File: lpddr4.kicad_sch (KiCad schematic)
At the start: 43 parts, among them U1 MT53E1G32D2NP-046

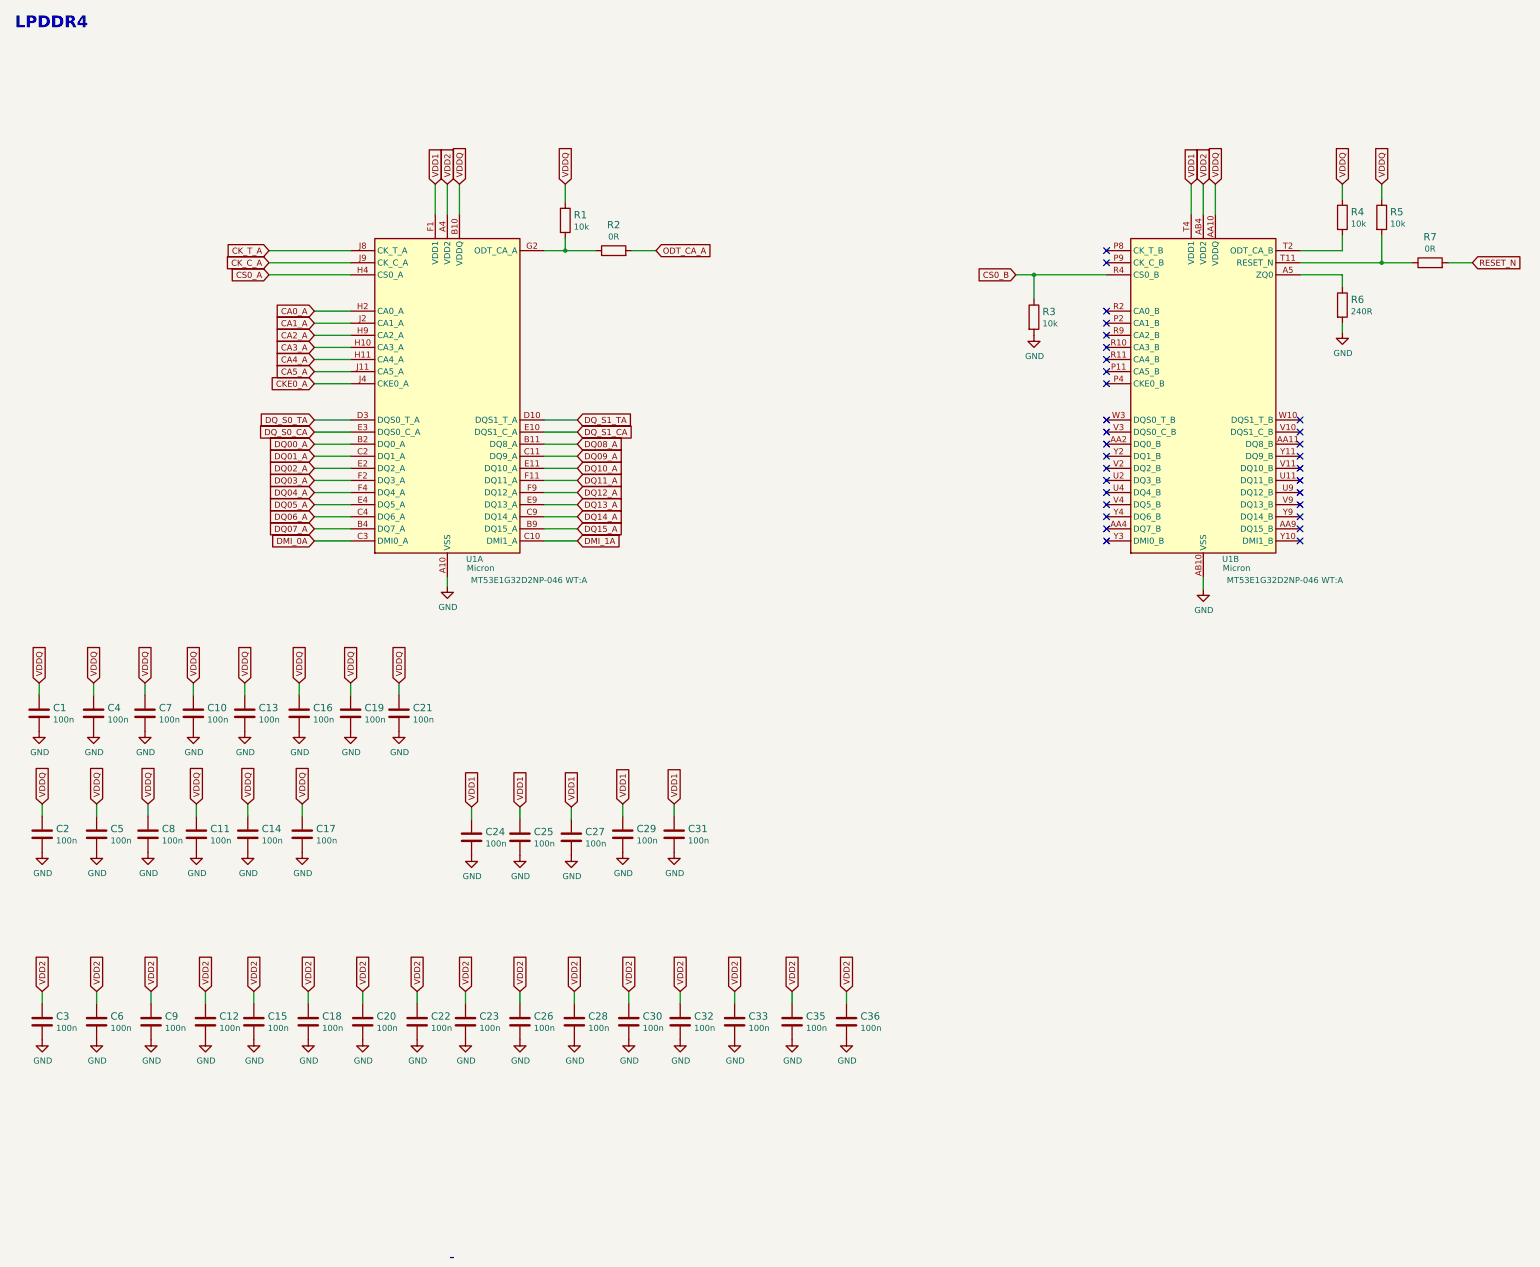
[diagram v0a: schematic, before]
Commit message: Update symbols from library, redo designators
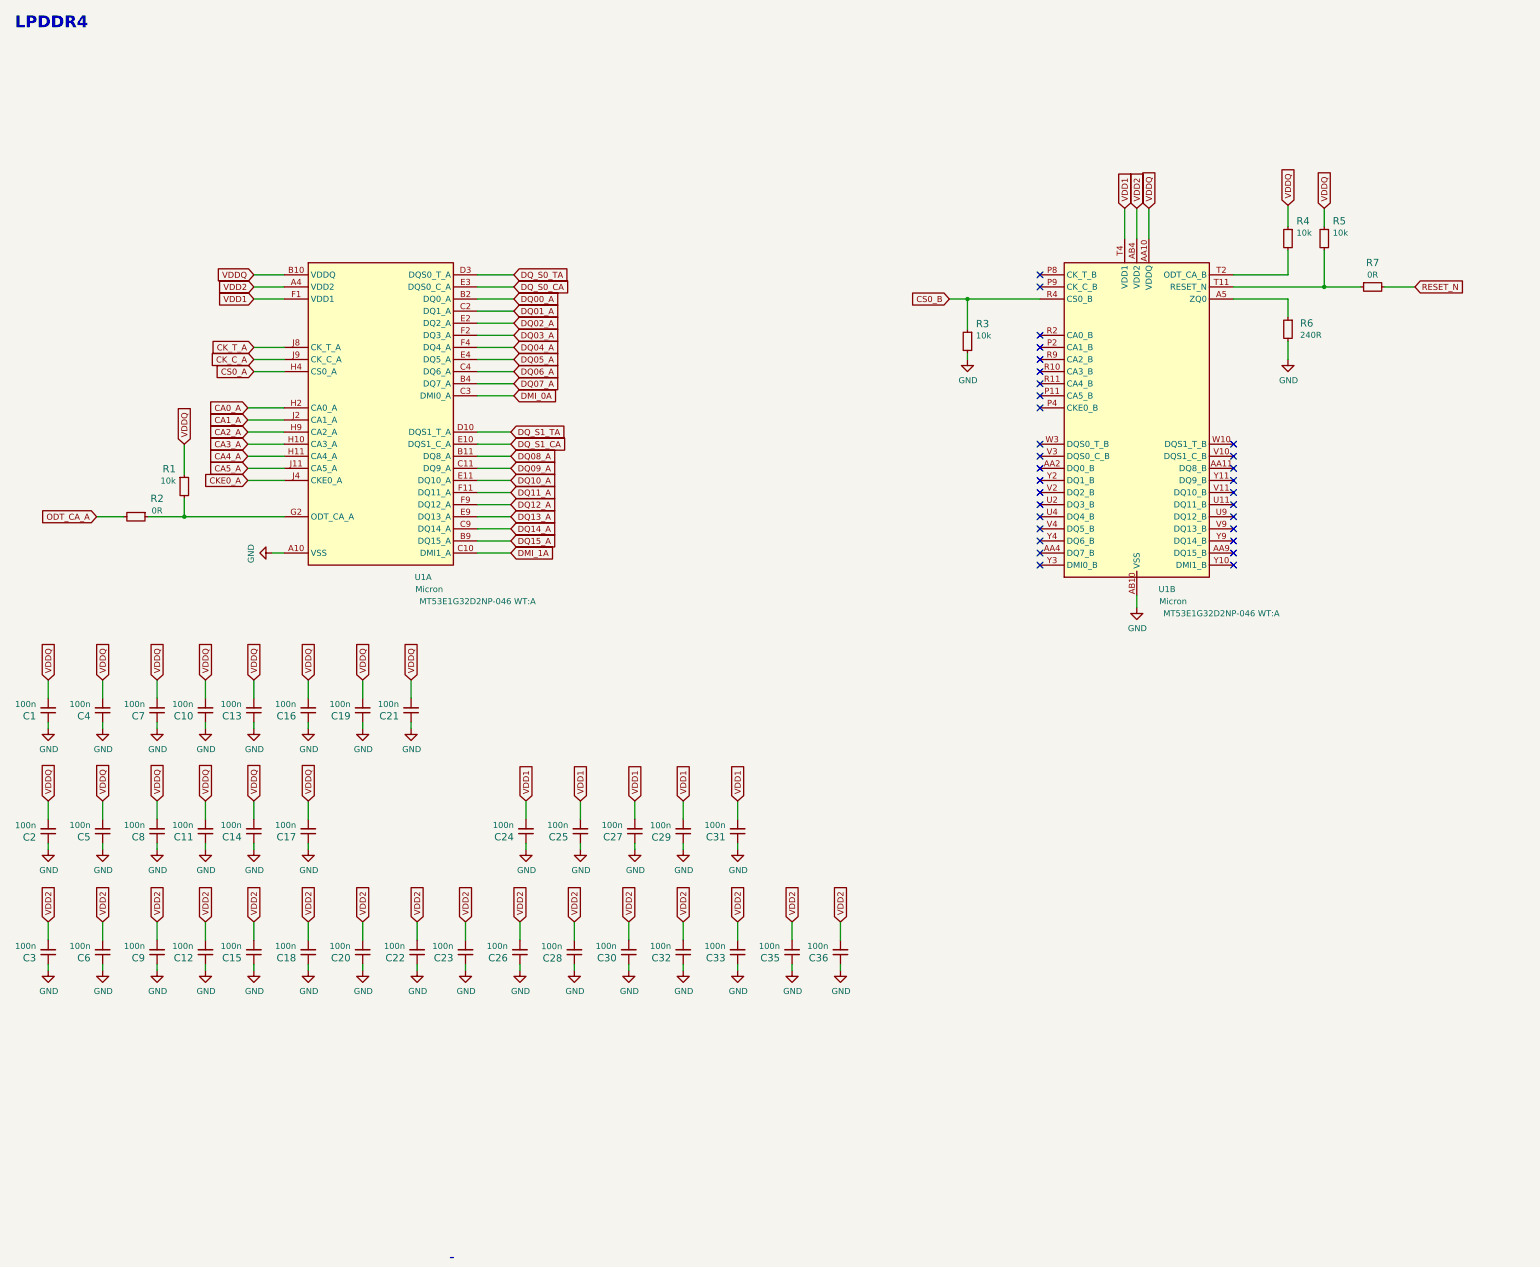
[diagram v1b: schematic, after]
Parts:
- C1, C10, C11, C12, C13, C14, C15, C16, C17, C18, C19, C2, C20, C21, C22, C23, C24, C25, C26, C27, C28, C29, C3, C30, C31, C32, C33, C35, C36, C4, C5, C6, C7, C8, C9: Author (none) -> Antmicro; License (none) -> Apache-2.0; Manufacturer YAGEO -> Yaego
- R1, R3, R4, R5: Author (none) -> Antmicro; License (none) -> Apache-2.0; MPN CRCW040210K0FKEDHP -> CR0402-FX-1002GLF; Manufacturer VISHAY -> Bourns; Tolerance (none) -> 1%
- R2, R7: Author (none) -> Antmicro; Current (none) -> 1A; License (none) -> Apache-2.0; Manufacturer PANASONIC -> Panasonic
- R6: Author (none) -> Antmicro; License (none) -> Apache-2.0; MPN ERJ2GEJ241X -> CR0402-FX-2400GLF; Manufacturer PANASONIC -> Bourns; Tolerance (none) -> 1%
- U1: Author (none) -> Antmicro; License (none) -> Apache-2.0
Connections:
- net GND: now also C1.1, C10.1, C11.1, C12.1, C13.1, C14.1, C15.1, C16.1, C17.1, C18.1, C19.1, C2.1, C20.1, C21.1, C22.1, C23.1, C24.1, C25.1, C26.1, C27.1, C28.1, C29.1, C3.1, C30.1, C31.1, C32.1, C33.1, C35.1, C36.1, C4.1, C5.1, C6.1, C7.1, C8.1, C9.1; no longer C1.2, C10.2, C11.2, C12.2, C13.2, C14.2, C15.2, C16.2, C17.2, C18.2, C19.2, C2.2, C20.2, C21.2, C22.2, C23.2, C24.2, C25.2, C26.2, C27.2, C28.2, C29.2, C3.2, C30.2, C31.2, C32.2, C33.2, C35.2, C36.2, C4.2, C5.2, C6.2, C7.2, C8.2, C9.2
- net VDD1: now also C24.2, C25.2, C27.2, C29.2, C31.2; no longer C24.1, C25.1, C27.1, C29.1, C31.1
- net VDD2: now also C12.2, C15.2, C18.2, C20.2, C22.2, C23.2, C26.2, C28.2, C3.2, C30.2, C32.2, C33.2, C35.2, C36.2, C6.2, C9.2; no longer C12.1, C15.1, C18.1, C20.1, C22.1, C23.1, C26.1, C28.1, C3.1, C30.1, C32.1, C33.1, C35.1, C36.1, C6.1, C9.1
- net VDDQ: now also C1.2, C10.2, C11.2, C13.2, C14.2, C16.2, C17.2, C19.2, C2.2, C21.2, C4.2, C5.2, C7.2, C8.2; no longer C1.1, C10.1, C11.1, C13.1, C14.1, C16.1, C17.1, C19.1, C2.1, C21.1, C4.1, C5.1, C7.1, C8.1
- net at U1.AA1 (DNU): now also U1.AA12 (DNU), U1.AB1 (DNU), U1.AB11 (DNU), U1.AB12 (DNU), U1.AB2 (DNU)
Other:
- moved on the sheet: C1, C10, C11, C12, C13, C14, C15, C16, C17, C18, C19, C2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
